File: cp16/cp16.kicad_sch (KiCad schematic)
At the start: 26 parts, among them J1 Conn_01x04, J2 Conn_01x04, SW1 SW_Push, SW10 SW_Push, SW11 SW_Push, SW12 SW_Push, SW13 SW_Push, SW14 SW_Push, SW15 SW_Push, SW16 SW_Push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

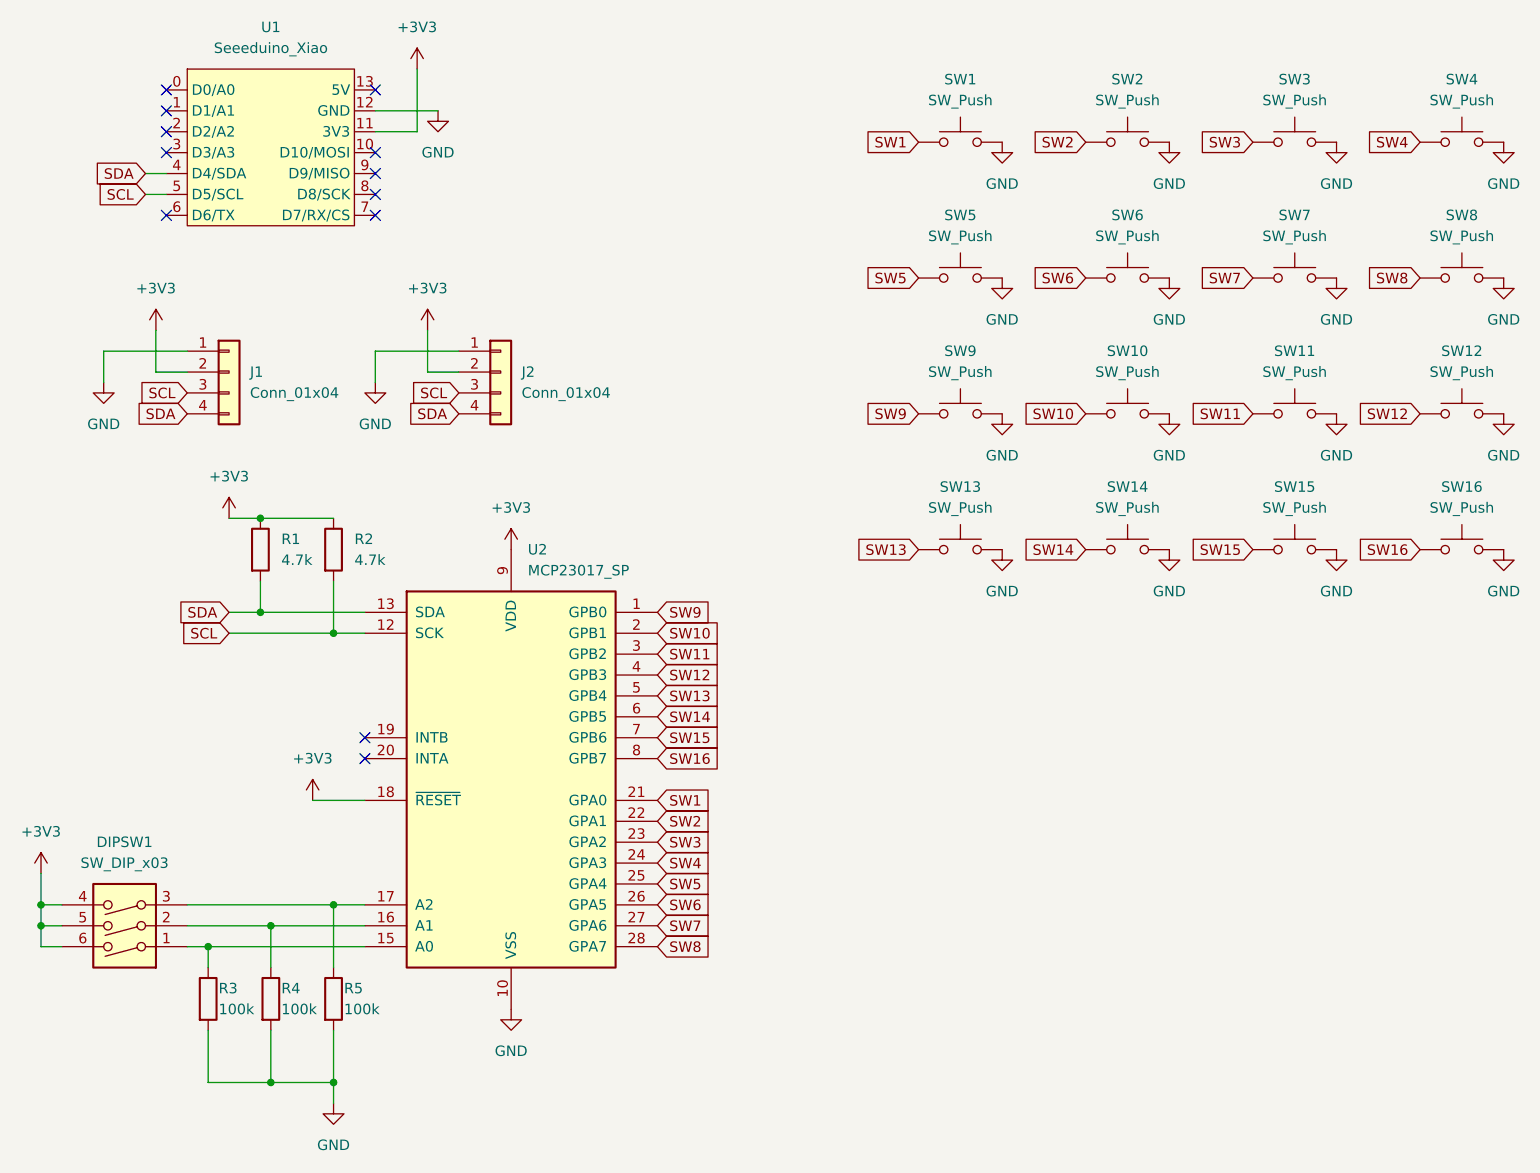
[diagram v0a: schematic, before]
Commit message: Layout parts
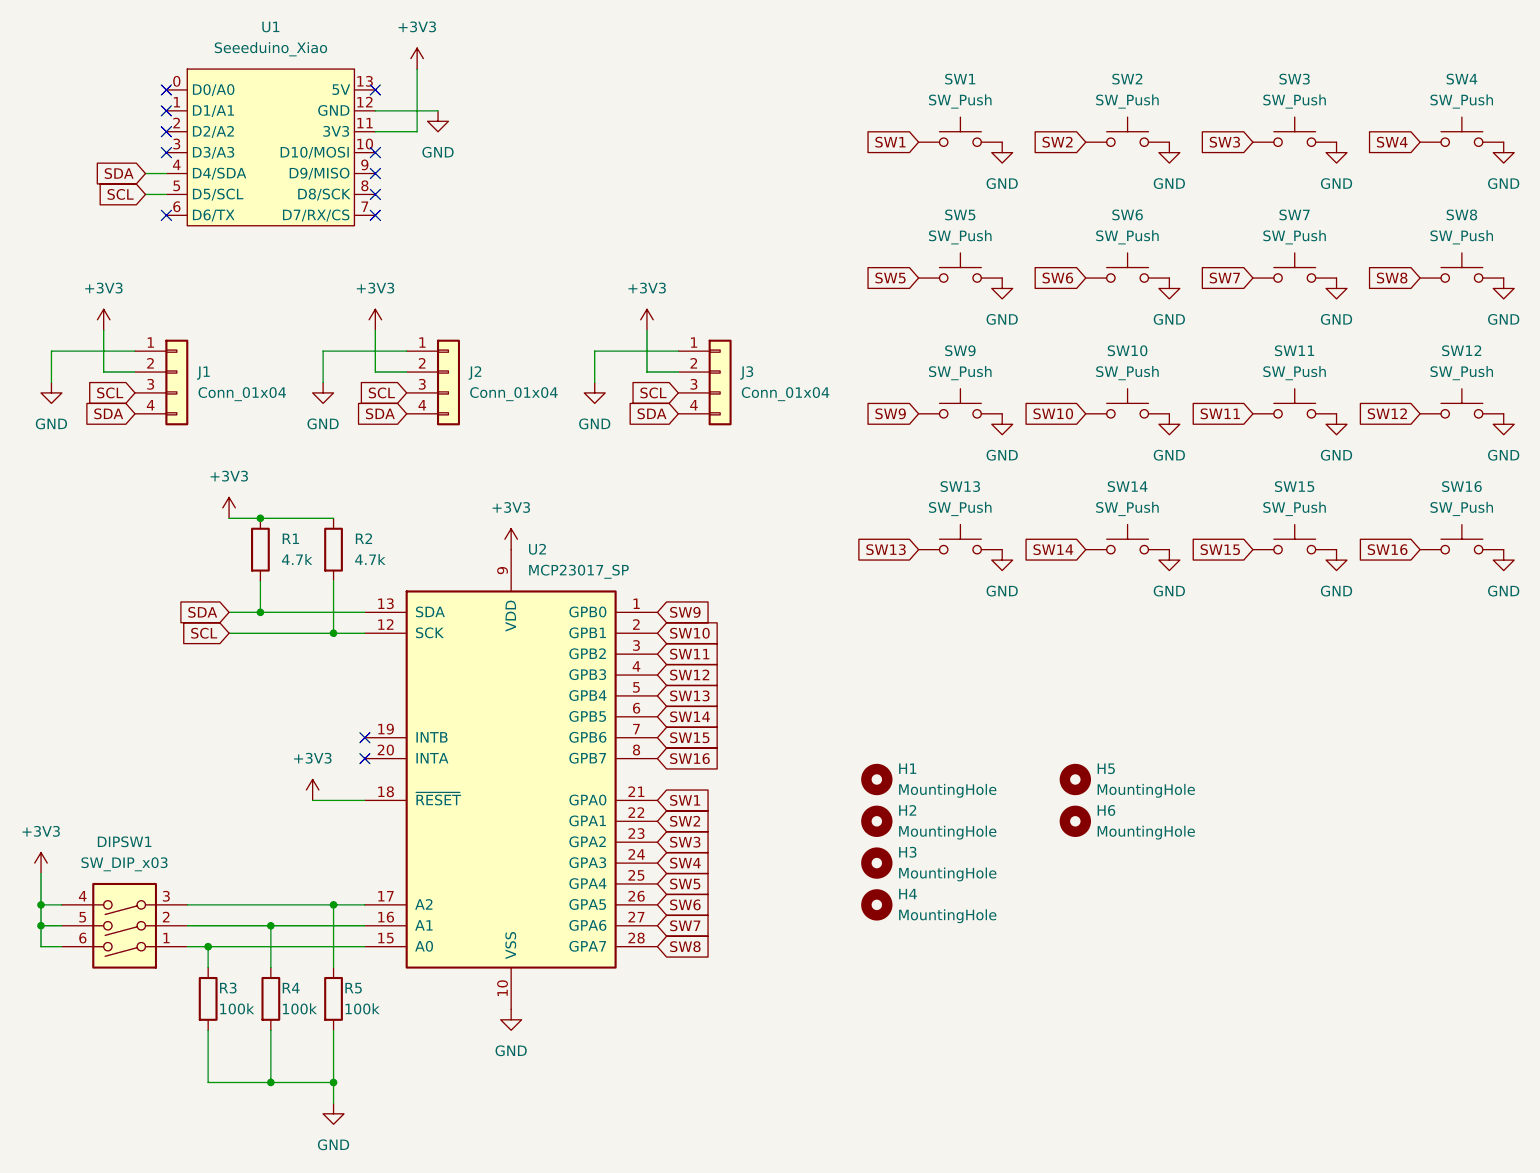
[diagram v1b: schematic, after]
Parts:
- added H1, H2, H3, H4: MountingHole, foostan_kbd:M2_HOLE_v2, symbol Mechanical:MountingHole
- added H5, H6: MountingHole, 1m38_kbd:M2_ScrewHole, symbol Mechanical:MountingHole
- added J3: Conn_01x04, 1m38_kbd:PinHeader_P2.54mm_I2C, symbol Connector_Generic:Conn_01x04
- J1, J2: footprint Connector_PinHeader_2.54mm:PinHeader_1x04_P2.54mm_Vertical -> 1m38_kbd:PinHeader_P2.54mm_I2C
- SW1, SW10, SW11, SW12, SW13, SW14, SW15, SW16, SW2, SW3, SW4, SW5, SW6, SW7, SW8, SW9: footprint (none) -> 1m38_kbd:CherryMX_MidHeight_Choc_Hotswap_mod
- U2: footprint Package_DIP:DIP-28_W7.62mm -> Package_DIP:DIP-28_W7.62mm_Socket
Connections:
- net +3V3: now also J3.2 (Pin_2)
- net GND: now also J3.1 (Pin_1)
- net SCL: now also J3.3 (Pin_3)
- net SDA: now also J3.4 (Pin_4)
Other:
- moved on the sheet: J1, J2

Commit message: Routing
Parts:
- U2: footprint Package_DIP:DIP-28_W7.62mm_Socket -> Package_DIP:DIP-28_W7.62mm
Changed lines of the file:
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@@
       (effects (font (size 1.27 1.27)) (justify left))
     )
-    (property "Footprint" "Package_DIP:DIP-28_W7.62mm_Socket" (id 2) (at 85.09 137.16 0)
+    (property "Footprint" "Package_DIP:DIP-28_W7.62mm" (id 2) (at 85.09 137.16 0)
       (effects (font (size 1.27 1.27)) (justify left) hide)
     )
@@
     )
     (path "/98060f6a-0fd9-43a5-abcd-87e9cb83ea41"
-      (reference "U2") (unit 1) (value "MCP23017_SP") (footprint "Package_DIP:DIP-28_W7.62mm_Socket")
-    )
-  )
+      (reference "U2") (unit 1) (value "MCP23017_SP") (footprint "Package_DIP:DIP-28_W7.62mm")
+    )
+  )
